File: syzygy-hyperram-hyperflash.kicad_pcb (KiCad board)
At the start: 4 copper layers, 45 x 41.9 mm, 36 parts, among them IC1 ATTINY44A-MMH, IC2 TLV6710DDCT, IC3 S27KL0641DABHI020, IC4 S71KL256SC0BHI, J1 SYZYGY_STD, J2 Conn_02x03_Odd_Even, J3 Conn_02x03_Odd_Even

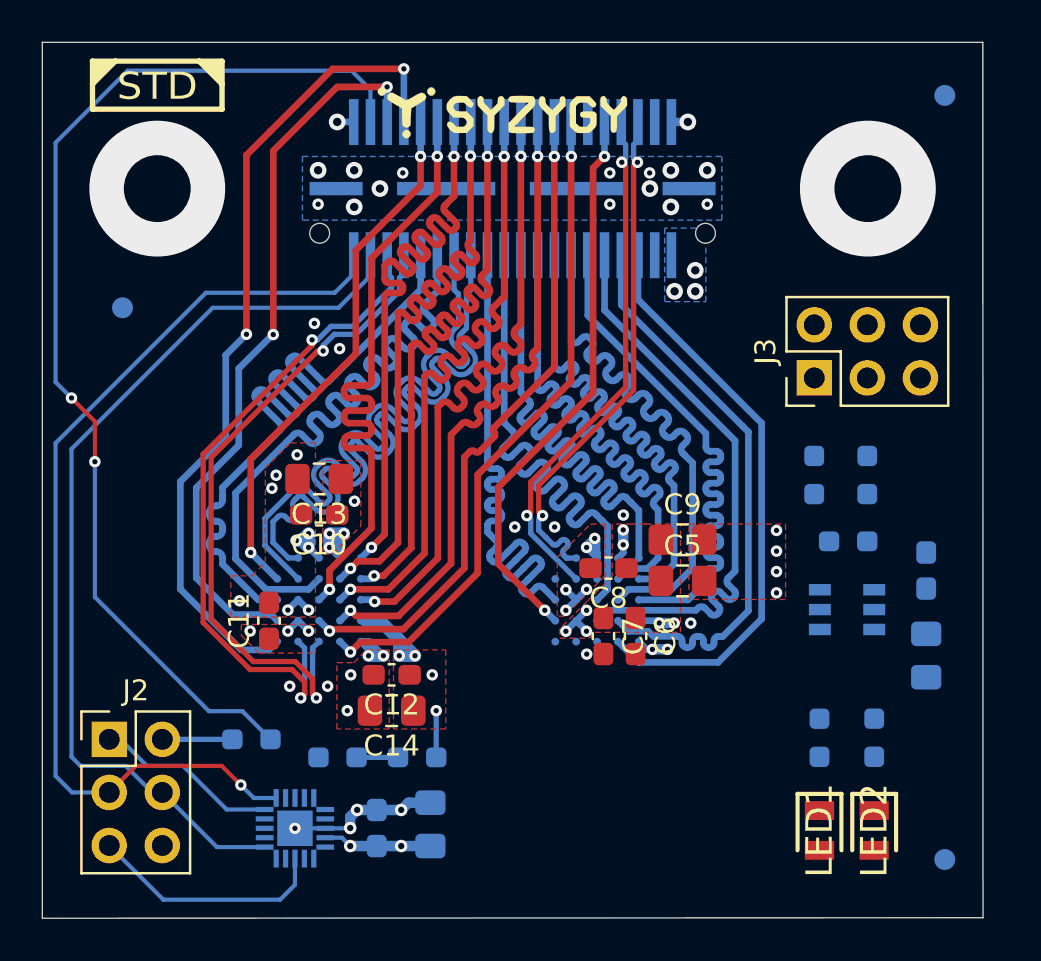
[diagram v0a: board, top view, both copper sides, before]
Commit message: Route all non-power / non-plane signals
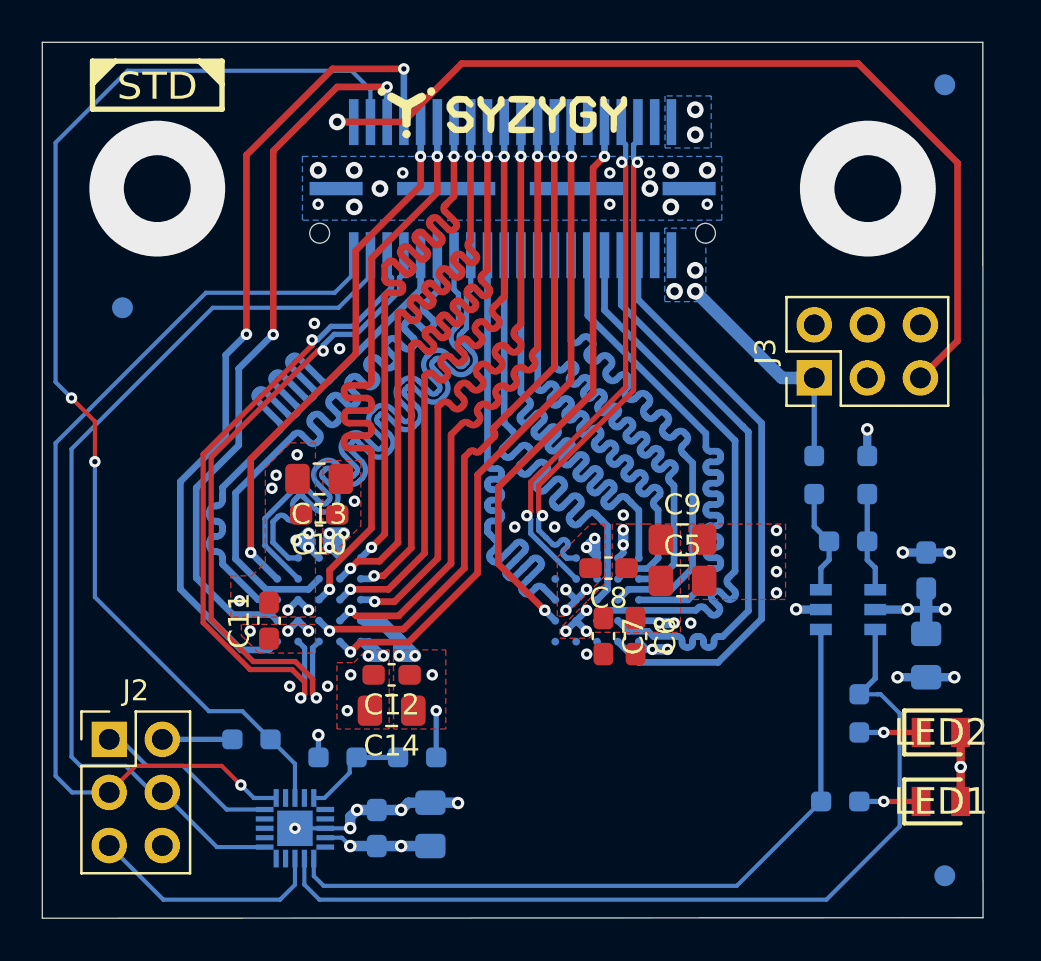
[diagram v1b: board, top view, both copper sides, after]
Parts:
- moved LED1 5.97 mm to (144.6, 89.6), turned to 0 degrees
- moved LED2 5.67 mm to (144.6, 86.3), turned to 0 degrees
- moved R2 3.20 mm to (139.8, 89.6), turned to 180 degrees
- moved R3 1.37 mm to (140.7, 85.4)
- moved FID8 0.78 mm to (144.8, 93.2)
- moved FID6 0.51 mm to (144.8, 55.3)
- moved IC2 0.05 mm to (140.2, 80.5)
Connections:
- IC1 pad 11: unconnected-(IC1-PB0_(PCINT8/XTAL1/CLKI)-Pad11) -> /VIO_UV
- IC1 pad 12: unconnected-(IC1-PB1_(PCINT9/XTAL2)-Pad12) -> /VIO_OV
- IC1 pad 2: /VIO_OV -> unconnected-(IC1-(ADC3/T0/PCINT3)_PA3-Pad2)
- IC1 pad 3: /VIO_UV -> /RGA
- IC1 pad 4: /VIO_sense -> unconnected-(IC1-(ADC1/AIN0/PCINT1)_PA1-Pad4)
- IC1 pad 5: /RGA -> /VIO_sense
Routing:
- net +5V: track 0.79 -> 44.6 mm
- net /VIO_OV: track 0.00 -> 42.6 mm
- net /VIO_UV: track 0.00 -> 35.2 mm
- net VCC: track 19.3 -> 30.4 mm
- net GND: track 21.8 -> 31.6 mm, vias 51 -> 59
- net +3.3V: track 9.34 -> 17.4 mm, vias 3 -> 7
- net Net-(IC2-INA): track 0.00 -> 5.03 mm
- net Net-(IC2-INB): track 0.00 -> 4.74 mm
- net /RGA: track 52.2 -> 55.5 mm
- net /VIO_sense: track 1.98 -> 5.08 mm
- net Net-(LED2-Pad1): track 0.00 -> 2.95 mm, vias 0 -> 1
- net Net-(LED1-Pad1): track 0.00 -> 2.95 mm, vias 0 -> 1
- added copper zone on B.Cu, net +3.3V
